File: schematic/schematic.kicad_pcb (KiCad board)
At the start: 2 copper layers, 34 x 35.8 mm, 18 parts, among them Q3 2N7000, SW1 PAIRING, U1 MCP4161-xxxx-P, U2 MCP4161-xxxx-P, U3 ESP32-WROOM-32E, U4 MCP4161-xxxx-P, U5 MCP4161-xxxx-P, U6 74HCT245

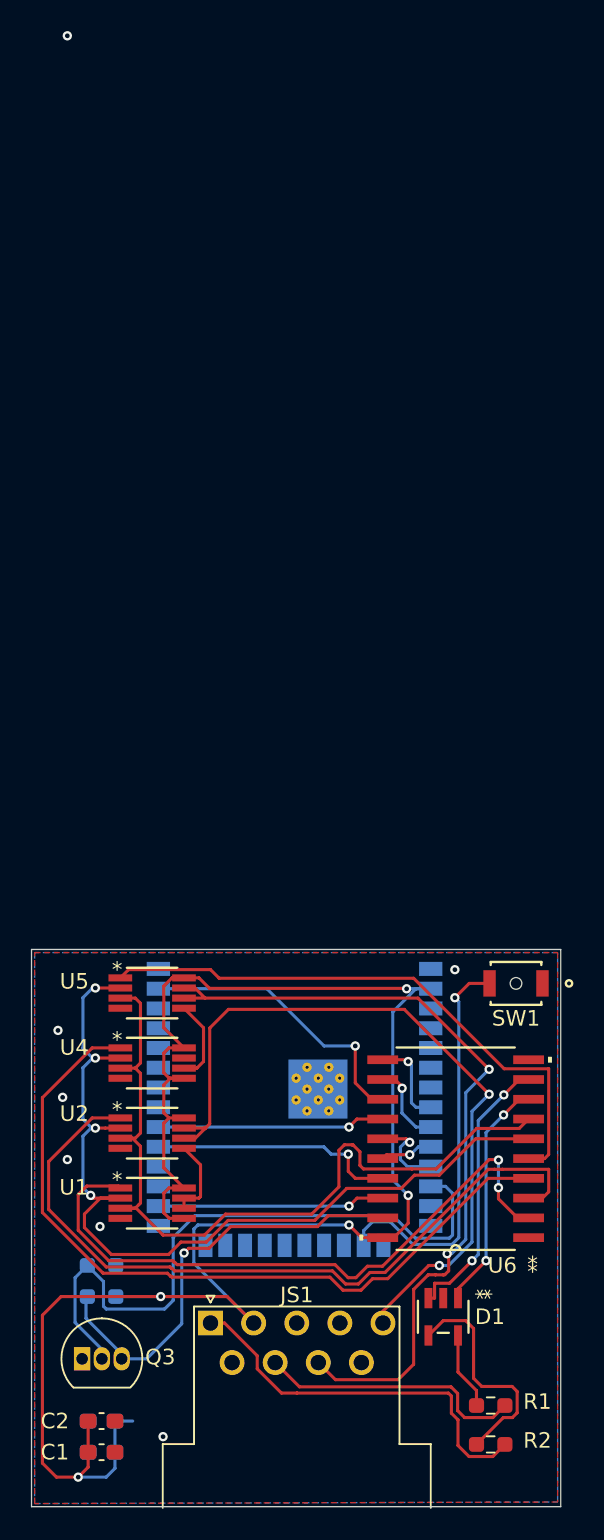
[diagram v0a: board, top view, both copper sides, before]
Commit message: maybe fixed caps, made space for de9 jackscrews
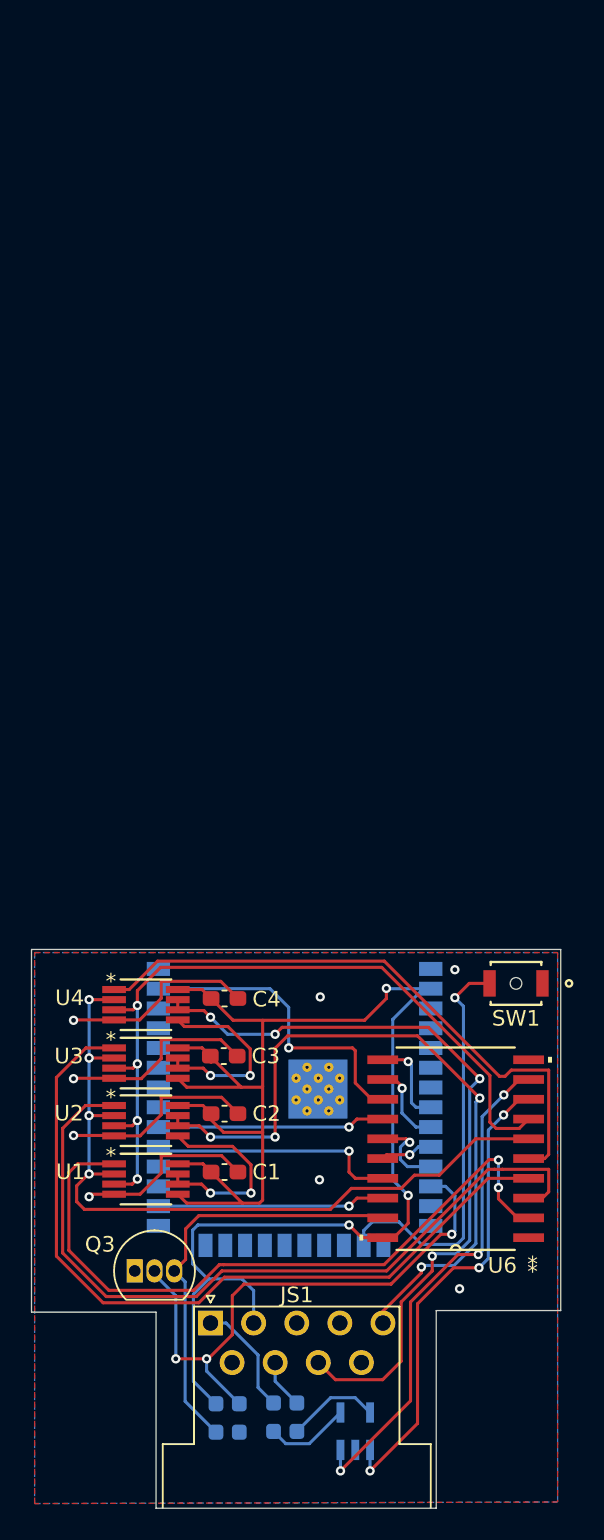
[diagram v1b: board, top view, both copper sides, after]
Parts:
- C3, C4: moved to F.Cu
- D1, R1, R2: moved to B.Cu
- moved C4 28.3 mm to (113.9, 61.9), turned to 0 degrees
- moved C3 26.6 mm to (113.8, 65.5), turned to 0 degrees
- moved C2 21.3 mm to (113.9, 69.2)
- moved C1 19.7 mm to (113.9, 73.0)
- moved R2 14.1 mm to (117.0, 88.8), turned to 90 degrees
- moved R3 13.2 mm to (114.8, 88.8), turned to -90 degrees
- moved R1 12.5 mm to (118.5, 88.8), turned to 90 degrees
- moved R4 10.7 mm to (113.3, 88.8), turned to 90 degrees
- moved D1 9.27 mm to (122.3, 89.7), turned to 90 degrees
- moved Q3 6.58 mm to (108.1, 79.3)
- moved U1 1.60 mm to (108.8, 73.5)
- moved U2 0.89 mm to (108.8, 69.7)
- moved U4 0.85 mm to (108.8, 62.2)
- moved U3 0.40 mm to (108.8, 66.0)
- renumbered R5 to R3, R6 to R4, U4 to U3, U5 to U4, U3 to U5
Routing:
- net /GND: track 0.00 -> 49.8 mm, vias 7 -> 8
- net /GAMESW1: track 24.9 -> 7.80 mm
- net Net-(U6-A6): track 15.0 -> 30.8 mm, vias 2 -> 3
- net Net-(U6-A7): track 17.9 -> 32.6 mm, vias 2 -> 3
- net /GAMESW0: track 17.2 -> 3.18 mm
- net /+5V: track 120.3 -> 108.0 mm, vias 5 -> 3
- net Net-(D1-CATHODE-Pad4): track 14.7 -> 5.45 mm
- net Net-(U1-P0B): track 5.29 -> 12.9 mm, vias 0 -> 2
- net Net-(U1-SCK): track 58.3 -> 50.9 mm
- net Net-(U3-P0B): track 5.38 -> 12.6 mm, vias 0 -> 2
- net Net-(Q3-G): track 42.4 -> 36.8 mm, vias 0 -> 3
- net Net-(U1-~{CS}): track 41.6 -> 45.2 mm
- net /PDL0: track 48.6 -> 46.2 mm, vias 2 -> 4
- net /PDL1: track 51.9 -> 49.7 mm, vias 2 -> 4
- net Net-(U2-~{CS}): track 48.9 -> 50.6 mm
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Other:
- board size 34 x 35.8 mm -> 34 x 35.9 mm
